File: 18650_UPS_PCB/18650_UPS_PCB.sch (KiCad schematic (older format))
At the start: 44 parts, among them J1 USB_B_Micro, J2 Conn_01x02, J3 Conn_01x02, SW1 SW_DIP_x02, U1 STLINK-V3MINI, U10 LR9102G-xx, U11 MP2667, U2 INA237, U3 EA_DOGS104N-A, U5 STM32L151RCTx

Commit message: Major Overhaul
Changed Buttons, Display changed to OLED and moved to top PCB
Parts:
- removed C2, C3: 1 uF, Capacitor_SMD:C_0603_1608Metric, symbol Device:C_Small
- removed JP1: INA_ADR_0, Jumper:SolderJumper-3_P1.3mm_Open_RoundedPad1.0x1.5mm, symbol Jumper:SolderJumper_3_Open
- removed JP2: INA_ADR_1, Jumper:SolderJumper-3_P1.3mm_Open_RoundedPad1.0x1.5mm, symbol Jumper:SolderJumper_3_Open
- removed JP3: EA_ADR, Jumper:SolderJumper-3_P1.3mm_Open_RoundedPad1.0x1.5mm, symbol Jumper:SolderJumper_3_Open
- removed S1: TM-2027, CUSTOM_FOOTPRINTS:TM-2027, symbol CUSTOM_PARTS:TM-2027
- removed SW1: SW_DIP_x02, CUSTOM_FOOTPRINTS:TS6637TP-4P, symbol Switch:SW_DIP_x02
- removed U3: EA_DOGS104N-A, CUSTOM_FOOTPRINTS:EA_DOGS104N-A, symbol CUSTOM_PARTS:EA_DOGS104N-A
- added R6: 100 kOhm, Resistor_SMD:R_0603_1608Metric, symbol Device:R_Small
- added SW1: SW_SPST, CUSTOM_FOOTPRINTS:ALPSALPINE_SKPMDAE011, symbol Switch:SW_SPST
- added TP1, TP2, TP3, TP4: TestPoint, TestPoint:TestPoint_Pad_D2.5mm, symbol Connector:TestPoint
- added U3: BRIGHT_TSX103, CUSTOM_FOOTPRINTS:BRIGHT_TSX103, symbol CUSTOM_PARTS:BRIGHT_TSX103
- J2, J3: footprint Connector_PinSocket_2.54mm:PinSocket_1x02_P2.54mm_Vertical -> CUSTOM_FOOTPRINTS:Pin_Socket_SMD_Horizontal_1x2
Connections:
- wire segments 239 -> 215
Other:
- note removed: "LCD Textdisplay"
- moved on the sheet: C11

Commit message: Started routing V3
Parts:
- removed U3: BRIGHT_TSX103, CUSTOM_FOOTPRINTS:BRIGHT_TSX103, symbol CUSTOM_PARTS:BRIGHT_TSX103
- added S1: TM-2027, CUSTOM_FOOTPRINTS:TM-2027, symbol CUSTOM_PARTS:TM-2027
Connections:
- net GND: now also J3.1 (Pin_1), S1.4 (Common); no longer J3.2 (Pin_2)
- net I2C1_SCL: now also U5.61 (PB8); no longer U5.29 (PB10)
- net I2C1_SDA: now also U5.62 (PB9); no longer U5.30 (PB11)
- net MP-INT: now also U5.38 (PC7); no longer U5.8 (PC0)
- net TM-A: now also U5.36 (PB15), S1.1 (A); no longer U5.22 (PA6)
- net TM-B: now also U5.35 (PB14), S1.2 (B); no longer U5.21 (PA5)
- net TM-C: now also U5.34 (PB13), S1.3 (C); no longer U5.20 (PA4)
- net TM-Center: now also U5.37 (PC6), S1.6 (Center); no longer U5.23 (PA7)
- net TM-D: now also U5.33 (PB12), S1.5 (D); no longer U5.17 (PA3)
- net VSS: now also J3.2 (Pin_2); no longer J3.1 (Pin_1)
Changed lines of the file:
@@
 	1    0    0    -1
 $EndComp
-Text GLabel 13150 3750 0    50   Input ~ 0
+Text GLabel 13150 4450 0    50   Input ~ 0
 MP-INT
 Text GLabel 14700 4450 2    50   Input ~ 0
@@
 Text GLabel 14700 2850 2    50   Input ~ 0
 EA-RST
-Text GLabel 4750 6650 1    50   Input ~ 0
+Text GLabel 4800 6800 1    50   Input ~ 0
 TM-A
 Wire Wire Line
-	4750 6650 4750 6700
-Wire Wire Line
-	4400 7000 4300 7000
-Wire Wire Line
-	4750 7600 4750 7700
-Wire Wire Line
-	4400 7200 4250 7200
-Text GLabel 4300 7000 0    50   Input ~ 0
+	4800 6800 4800 6850
+Wire Wire Line
+	4350 7150 4250 7150
+Wire Wire Line
+	4800 7650 4800 7750
+Wire Wire Line
+	5250 7350 5400 7350
+Text GLabel 4250 7150 0    50   Input ~ 0
 TM-B
-Text GLabel 5200 7000 2    50   Input ~ 0
+Text GLabel 5350 7150 2    50   Input ~ 0
 TM-D
-Text GLabel 4750 7700 3    50   Input ~ 0
+Text GLabel 4800 7750 3    50   Input ~ 0
 TM-C
 $Comp
 L power:GND #PWR0123
 U 1 1 61502D4C
-P 4200 7400
-F 0 "#PWR0123" H 4200 7150 50  0001 C CNN
-F 1 "GND" H 4205 7227 50  0000 C CNN
-F 2 "" H 4200 7400 50  0001 C CNN
-F 3 "" H 4200 7400 50  0001 C CNN
-	1    4200 7400
-	1    0    0    -1
-$EndComp
-Wire Wire Line
-	4200 7300 4200 7400
-Wire Wire Line
-	4200 7300 4400 7300
-Text GLabel 14700 2650 2    50   Input ~ 0
+P 4150 7450
+F 0 "#PWR0123" H 4150 7200 50  0001 C CNN
+F 1 "GND" H 4155 7277 50  0000 C CNN
+F 2 "" H 4150 7450 50  0001 C CNN
+F 3 "" H 4150 7450 50  0001 C CNN
+	1    4150 7450
+	1    0    0    -1
+$EndComp
+Wire Wire Line
+	4150 7350 4150 7450
+Wire Wire Line
+	4150 7350 4350 7350
+Text GLabel 14700 5250 2    50   Input ~ 0
 TM-A
-Text GLabel 14700 2550 2    50   Input ~ 0
+Text GLabel 14700 5150 2    50   Input ~ 0
 TM-B
-Text GLabel 14700 2450 2    50   Input ~ 0
+Text GLabel 14700 5050 2    50   Input ~ 0
 TM-C
-Text GLabel 14700 2350 2    50   Input ~ 0
+Text GLabel 14700 4950 2    50   Input ~ 0
 TM-D
-Text GLabel 14700 2750 2    50   Input ~ 0
+Text GLabel 13200 4350 0    50   Input ~ 0
 TM-Center
 Text Notes 3800 6450 0    50   ~ 0
@@
 	14700 4450 14600 4450
 Wire Wire Line
-	14700 2750 14600 2750
-Wire Wire Line
-	14600 2650 14700 2650
-Wire Wire Line
-	14700 2550 14600 2550
-Wire Wire Line
-	14600 2450 14700 2450
-Wire Wire Line
-	14700 2350 14600 2350
-Wire Wire Line
-	13150 3750 13300 3750
+	13200 4350 13300 4350
+Wire Wire Line
+	14600 5250 14700 5250
+Wire Wire Line
+	14700 5150 14600 5150
+Wire Wire Line
+	14600 5050 14700 5050
+Wire Wire Line
+	14700 4950 14600 4950
+Wire Wire Line
+	13150 4450 13300 4450
 Wire Wire Line
 	13300 3850 13150 3850
@@
 NoConn ~ 13300 4650
 NoConn ~ 13300 4550
-NoConn ~ 13300 4450
-NoConn ~ 13300 4350
+NoConn ~ 13200 3750
+NoConn ~ 14700 2750
 NoConn ~ 13300 4250
 NoConn ~ 13300 4150
@@
 L Connector_Generic:Conn_01x02 J3
 U 1 1 610BC06E
-P 4200 9750
-F 0 "J3" H 4280 9742 50  0000 L CNN
-F 1 "Conn_01x02" H 4280 9651 50  0000 L CNN
-F 2 "CUSTOM_FOOTPRINTS:Pin_Socket_SMD_Horizontal_1x2" H 4200 9750 50  0001 C CNN
-F 3 "~" H 4200 9750 50  0001 C CNN
-	1    4200 9750
-	1    0    0    -1
+P 4200 9850
+F 0 "J3" H 4280 9842 50  0000 L CNN
+F 1 "Conn_01x02" H 4280 9751 50  0000 L CNN
+F 2 "CUSTOM_FOOTPRINTS:Pin_Socket_SMD_Horizontal_1x2" H 4200 9850 50  0001 C CNN
+F 3 "~" H 4200 9850 50  0001 C CNN
+	1    4200 9850
+	1    0    0    1
 $EndComp
 $Comp
@@
 Wire Notes Line
 	15850 700  15850 6200
-Text GLabel 14700 4850 2    50   Input ~ 0
+Text GLabel 14700 4650 2    50   Input ~ 0
 I2C1_SDA
-Text GLabel 14700 4750 2    50   Input ~ 0
+Text GLabel 14700 4550 2    50   Input ~ 0
 I2C1_SCL
 Text GLabel 5450 4950 3    50   Input ~ 0
@@
 	5450 4650 5450 4950
 Wire Wire Line
-	14700 4750 14600 4750
-Wire Wire Line
-	14600 4850 14700 4850
+	14700 4550 14600 4550
+Wire Wire Line
+	14600 4650 14700 4650
 NoConn ~ 14700 2950
 NoConn ~ 14700 3050
@@
 NoConn ~ 14700 4150
 NoConn ~ 14700 4250
-NoConn ~ 14700 4550
-NoConn ~ 14700 4650
-NoConn ~ 14700 4950
-NoConn ~ 14700 5050
-NoConn ~ 14700 5150
-NoConn ~ 14700 5250
-Wire Wire Line
-	14600 5250 14700 5250
-Wire Wire Line
-	14600 5150 14700 5150
-Wire Wire Line
-	14600 5050 14700 5050
-Wire Wire Line
-	14700 4950 14600 4950
-Wire Wire Line
-	14700 4650 14600 4650
-Wire Wire Line
-	14700 4550 14600 4550
+NoConn ~ 14700 4750
+NoConn ~ 14700 4850
+NoConn ~ 14700 2350
+NoConn ~ 14700 2450
+NoConn ~ 14700 2550
+NoConn ~ 14700 2650
+Wire Wire Line
+	14600 2650 14700 2650
+Wire Wire Line
+	14600 2550 14700 2550
+Wire Wire Line
+	14600 2450 14700 2450
+Wire Wire Line
+	14700 2350 14600 2350
+Wire Wire Line
+	14700 4850 14600 4850
+Wire Wire Line
+	14700 4750 14600 4750
 Wire Wire Line
 	14700 4250 14600 4250
@@
 Wire Wire Line
 	2250 5150 3650 5150
-$Comp
-L CUSTOM_PARTS:BRIGHT_TSX103 U3
-U 1 1 6110E704
-P 4700 6450
-F 0 "U3" H 5100 5700 50  0000 L CNN
-F 1 "BRIGHT_TSX103" H 5100 5550 50  0000 L CNN
-F 2 "CUSTOM_FOOTPRINTS:BRIGHT_TSX103" H 4650 6450 50  0001 C CNN
-F 3 "" H 4650 6450 50  0001 C CNN
-	1    4700 6450
-	1    0    0    -1
-$EndComp
-Wire Wire Line
-	5100 7000 5200 7000
+Wire Wire Line
+	5250 7150 5350 7150
 $Comp
 L Device:R_Small R6
@@
 Text GLabel 6700 7100 2    50   Input ~ 0
 MP-INT
-Text GLabel 4250 7200 0    50   Input ~ 0
+Text GLabel 5400 7350 2    50   Input ~ 0
 TM-Center
+$Comp
+L CUSTOM_PARTS:TM-2027 S1
+U 1 1 61106E72
+P 4700 6900
+F 0 "S1" H 4950 6950 50  0000 C CNN
+F 1 "TM-2027" H 4500 6950 50  0000 C CNN
+F 2 "CUSTOM_FOOTPRINTS:TM-2027" H 5550 7050 50  0001 C CNN
+F 3 "" H 5050 6900 50  0001 C CNN
+	1    4700 6900
+	1    0    0    -1
+$EndComp
+Wire Wire Line
+	14700 2750 14600 2750
+Wire Wire Line
+	13200 3750 13300 3750
 $EndSCHEMATC

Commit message: Finished routing
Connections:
- net INA-ALERT: now also U5.43 (PA10); no longer U5.9 (PC1)
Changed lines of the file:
@@
 Text Notes 3800 6450 0    50   ~ 0
 Control
-Text GLabel 13150 3850 0    50   Input ~ 0
+Text GLabel 14750 3050 2    50   Input ~ 0
 INA-ALERT
 Wire Notes Line
@@
 	13150 4450 13300 4450
 Wire Wire Line
-	13300 3850 13150 3850
+	14600 3050 14750 3050
 Wire Wire Line
 	14700 2850 14600 2850
@@
 	14600 4650 14700 4650
 NoConn ~ 14700 2950
-NoConn ~ 14700 3050
+NoConn ~ 13200 3850
 NoConn ~ 14700 3150
 NoConn ~ 14700 3250
@@
 	14700 3150 14600 3150
 Wire Wire Line
-	14600 3050 14700 3050
+	13300 3850 13200 3850
 Wire Wire Line
 	14600 2950 14700 2950

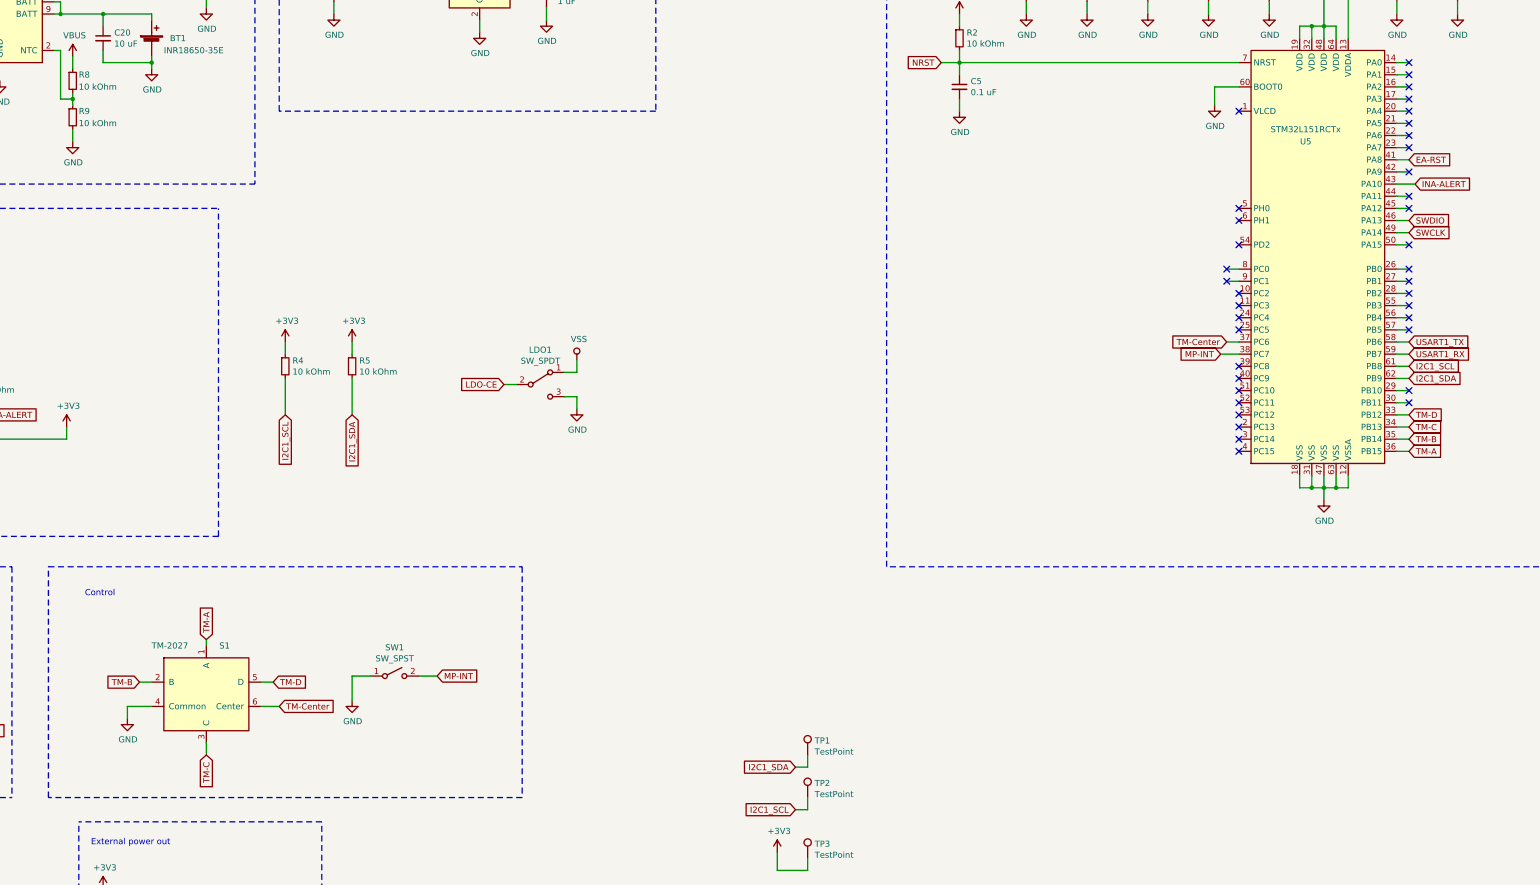
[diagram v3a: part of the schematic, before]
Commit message: changed buttons
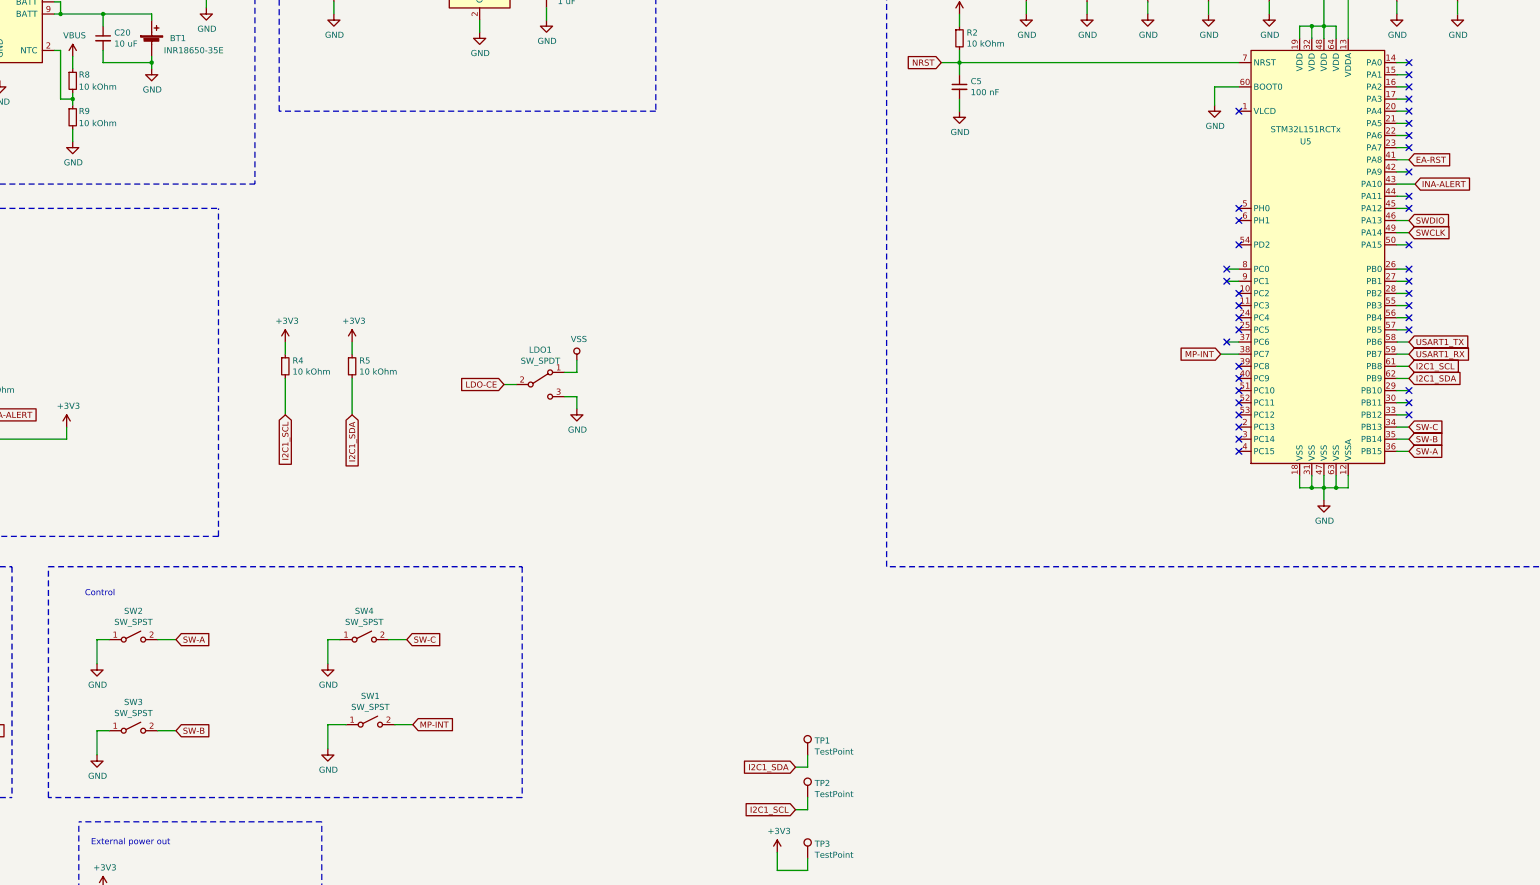
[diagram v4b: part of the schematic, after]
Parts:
- removed S1: TM-2027, CUSTOM_FOOTPRINTS:TM-2027, symbol CUSTOM_PARTS:TM-2027
- added SW2, SW3, SW4: SW_SPST, CUSTOM_FOOTPRINTS:PTS815, symbol Switch:SW_SPST
- C5: value 0.1 uF -> 100 nF
- C6, C8: footprint Capacitor_SMD:C_0805_2012Metric -> Capacitor_SMD:C_0603_1608Metric
- SW1: footprint CUSTOM_FOOTPRINTS:ALPSALPINE_SKPMDAE011 -> CUSTOM_FOOTPRINTS:PTS815
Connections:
- net GND: now also SW2.1 (A), SW3.1 (A), SW4.1 (A)
- net TM-A renamed SW-A
- net SW-A: now also SW2.2 (B)
- net TM-B renamed SW-B
- net SW-B: now also SW3.2 (B)
- net TM-C renamed SW-C
- net SW-C: now also SW4.2 (B)
- net TM-Center: no longer names the net of U5.37 (PC6)
- net TM-D: no longer names the net of U5.33 (PB12)
- no-connect marks 47 -> 49
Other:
- moved on the sheet: SW1
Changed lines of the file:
@@
 F 0 "C8" H 7692 1546 50  0000 L CNN
 F 1 "1 uF" H 7692 1455 50  0000 L CNN
-F 2 "Capacitor_SMD:C_0805_2012Metric" H 7600 1500 50  0001 C CNN
+F 2 "Capacitor_SMD:C_0603_1608Metric" H 7600 1500 50  0001 C CNN
 F 3 "~" H 7600 1500 50  0001 C CNN
 	1    7600 1500
@@
 F 0 "C6" H 5600 1500 50  0000 L CNN
 F 1 "1 uF" H 5450 1400 50  0000 L CNN
-F 2 "Capacitor_SMD:C_0805_2012Metric" H 5850 1450 50  0001 C CNN
+F 2 "Capacitor_SMD:C_0603_1608Metric" H 5850 1450 50  0001 C CNN
 F 3 "~" H 5850 1450 50  0001 C CNN
 	1    5850 1450
@@
 Text GLabel 14700 2850 2    50   Input ~ 0
 EA-RST
-Text GLabel 4800 6800 1    50   Input ~ 0
-TM-A
-Wire Wire Line
-	4800 6800 4800 6850
-Wire Wire Line
-	4350 7150 4250 7150
-Wire Wire Line
-	4800 7650 4800 7750
-Wire Wire Line
-	5250 7350 5400 7350
-Text GLabel 4250 7150 0    50   Input ~ 0
-TM-B
-Text GLabel 5350 7150 2    50   Input ~ 0
-TM-D
-Text GLabel 4800 7750 3    50   Input ~ 0
-TM-C
-$Comp
-L power:GND #PWR0123
-U 1 1 61502D4C
-P 4150 7450
-F 0 "#PWR0123" H 4150 7200 50  0001 C CNN
-F 1 "GND" H 4155 7277 50  0000 C CNN
-F 2 "" H 4150 7450 50  0001 C CNN
-F 3 "" H 4150 7450 50  0001 C CNN
-	1    4150 7450
-	1    0    0    -1
-$EndComp
-Wire Wire Line
-	4150 7350 4150 7450
-Wire Wire Line
-	4150 7350 4350 7350
-Text GLabel 14700 5250 2    50   Input ~ 0
-TM-A
-Text GLabel 14700 5150 2    50   Input ~ 0
-TM-B
-Text GLabel 14700 5050 2    50   Input ~ 0
-TM-C
-Text GLabel 14700 4950 2    50   Input ~ 0
-TM-D
-Text GLabel 13200 4350 0    50   Input ~ 0
-TM-Center
 Text Notes 3800 6450 0    50   ~ 0
 Control
@@
 AR Path="/613A65D4" Ref="C5"  Part="1"
 F 0 "C5" H 11092 2296 50  0000 L CNN
-F 1 "0.1 uF" H 11092 2205 50  0000 L CNN
+F 1 "100 nF" H 11092 2205 50  0000 L CNN
 F 2 "Capacitor_SMD:C_0603_1608Metric" H 11000 2250 50  0001 C CNN
 F 3 "~" H 11000 2250 50  0001 C CNN
@@
 Wire Wire Line
 	14700 4450 14600 4450
-Wire Wire Line
-	13200 4350 13300 4350
 Wire Wire Line
 	14600 5250 14700 5250
@@
 Wire Wire Line
 	2250 5150 3650 5150
-Wire Wire Line
-	5250 7150 5350 7150
 $Comp
 L Device:R_Small R6
@@
 Connection ~ 2000 1550
 Wire Wire Line
-	6000 7100 6000 7300
-Wire Wire Line
-	6150 7100 6000 7100
-Wire Wire Line
-	6700 7100 6550 7100
+	5800 7500 5800 7700
+Wire Wire Line
+	5950 7500 5800 7500
+Wire Wire Line
+	6500 7500 6350 7500
 $Comp
 L Switch:SW_SPST SW1
 U 1 1 61345DF7
-P 6350 7100
-F 0 "SW1" H 6350 7335 50  0000 C CNN
-F 1 "SW_SPST" H 6350 7244 50  0000 C CNN
-F 2 "CUSTOM_FOOTPRINTS:ALPSALPINE_SKPMDAE011" H 6350 7100 50  0001 C CNN
-F 3 "~" H 6350 7100 50  0001 C CNN
-	1    6350 7100
+P 6150 7500
+F 0 "SW1" H 6150 7735 50  0000 C CNN
+F 1 "SW_SPST" H 6150 7644 50  0000 C CNN
+F 2 "CUSTOM_FOOTPRINTS:PTS815" H 6150 7500 50  0001 C CNN
+F 3 "~" H 6150 7500 50  0001 C CNN
+	1    6150 7500
 	1    0    0    -1
 $EndComp
@@
 L power:GND #PWR0124
 U 1 1 61596BD9
-P 6000 7300
-F 0 "#PWR0124" H 6000 7050 50  0001 C CNN
-F 1 "GND" H 6005 7127 50  0000 C CNN
-F 2 "" H 6000 7300 50  0001 C CNN
-F 3 "" H 6000 7300 50  0001 C CNN
-	1    6000 7300
-	1    0    0    -1
-$EndComp
-Text GLabel 6700 7100 2    50   Input ~ 0
+P 5800 7700
+F 0 "#PWR0124" H 5800 7450 50  0001 C CNN
+F 1 "GND" H 5805 7527 50  0000 C CNN
+F 2 "" H 5800 7700 50  0001 C CNN
+F 3 "" H 5800 7700 50  0001 C CNN
+	1    5800 7700
+	1    0    0    -1
+$EndComp
+Text GLabel 6500 7500 2    50   Input ~ 0
 MP-INT
-Text GLabel 5400 7350 2    50   Input ~ 0
-TM-Center
-$Comp
-L CUSTOM_PARTS:TM-2027 S1
-U 1 1 61106E72
-P 4700 6900
-F 0 "S1" H 4950 6950 50  0000 C CNN
-F 1 "TM-2027" H 4500 6950 50  0000 C CNN
-F 2 "CUSTOM_FOOTPRINTS:TM-2027" H 5550 7050 50  0001 C CNN
-F 3 "" H 5050 6900 50  0001 C CNN
-	1    4700 6900
-	1    0    0    -1
-$EndComp
 Wire Wire Line
 	14700 2750 14600 2750
 Wire Wire Line
 	13200 3750 13300 3750
+$Comp
+L power:GND #PWR0119
+U 1 1 6111C509
+P 3900 7000
+F 0 "#PWR0119" H 3900 6750 50  0001 C CNN
+F 1 "GND" H 3905 6827 50  0000 C CNN
+F 2 "" H 3900 7000 50  0001 C CNN
+F 3 "" H 3900 7000 50  0001 C CNN
+	1    3900 7000
+	1    0    0    -1
+$EndComp
+Wire Wire Line
+	3900 7000 3900 6800
+Wire Wire Line
+	3900 6800 4000 6800
+Text GLabel 4550 6800 2    50   Input ~ 0
+SW-A
+Wire Wire Line
+	4400 6800 4550 6800
+$Comp
+L Switch:SW_SPST SW2
+U 1 1 61154FD9
+P 4200 6800
+F 0 "SW2" H 4200 7035 50  0000 C CNN
+F 1 "SW_SPST" H 4200 6944 50  0000 C CNN
+F 2 "CUSTOM_FOOTPRINTS:PTS815" H 4200 6800 50  0001 C CNN
+F 3 "~" H 4200 6800 50  0001 C CNN
+	1    4200 6800
+	1    0    0    -1
+$EndComp
+$Comp
+L power:GND #PWR0120
+U 1 1 6118A3A3
+P 3900 7750
+F 0 "#PWR0120" H 3900 7500 50  0001 C CNN
+F 1 "GND" H 3905 7577 50  0000 C CNN
+F 2 "" H 3900 7750 50  0001 C CNN
+F 3 "" H 3900 7750 50  0001 C CNN
+	1    3900 7750
+	1    0    0    -1
+$EndComp
+Wire Wire Line
+	3900 7750 3900 7550
+Wire Wire Line
+	3900 7550 4000 7550
+Text GLabel 4550 7550 2    50   Input ~ 0
+SW-B
+Wire Wire Line
+	4400 7550 4550 7550
+$Comp
+L Switch:SW_SPST SW3
+U 1 1 6118A3AD
+P 4200 7550
+F 0 "SW3" H 4200 7785 50  0000 C CNN
+F 1 "SW_SPST" H 4200 7694 50  0000 C CNN
+F 2 "CUSTOM_FOOTPRINTS:PTS815" H 4200 7550 50  0001 C CNN
+F 3 "~" H 4200 7550 50  0001 C CNN
+	1    4200 7550
+	1    0    0    -1
+$EndComp
+$Comp
+L power:GND #PWR0121
+U 1 1 61197B26
+P 5800 7000
+F 0 "#PWR0121" H 5800 6750 50  0001 C CNN
+F 1 "GND" H 5805 6827 50  0000 C CNN
+F 2 "" H 5800 7000 50  0001 C CNN
+F 3 "" H 5800 7000 50  0001 C CNN
+	1    5800 7000
+	1    0    0    -1
+$EndComp
+Wire Wire Line
+	5800 7000 5800 6800
+Wire Wire Line
+	5800 6800 5900 6800
+Text GLabel 6450 6800 2    50   Input ~ 0
+SW-C
+Wire Wire Line
+	6300 6800 6450 6800
+$Comp
+L Switch:SW_SPST SW4
+U 1 1 61197B30
+P 6100 6800
+F 0 "SW4" H 6100 7035 50  0000 C CNN
+F 1 "SW_SPST" H 6100 6944 50  0000 C CNN
+F 2 "CUSTOM_FOOTPRINTS:PTS815" H 6100 6800 50  0001 C CNN
+F 3 "~" H 6100 6800 50  0001 C CNN
+	1    6100 6800
+	1    0    0    -1
+$EndComp
+Text GLabel 14700 5250 2    50   Input ~ 0
+SW-A
+Text GLabel 14700 5150 2    50   Input ~ 0
+SW-B
+Text GLabel 14700 5050 2    50   Input ~ 0
+SW-C
+NoConn ~ 13200 4350
+Wire Wire Line
+	13200 4350 13300 4350
+NoConn ~ 14700 4950
 $EndSCHEMATC
